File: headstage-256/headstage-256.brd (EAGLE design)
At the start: 32 x 32 mm, 291 parts, among them J2 MMCX-J-P-H-ST-SM1/U.FL-R-SMT(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, J4 PINHD-2X5+4DF40-HEAD, J5 5041940270, U1 OPA170, U10 NRF24L01QFN, U11 CAT4016_QFN, U12 CAT4016_QFN, U13 TPL0501_UQFN, U14 TPL0501_UQFN, U15 MICROSD_473093751, U16 10M08SAM15317G, U17 Si8487DB, U18 MAX17048_WLP, U19 BNO055, U2 OPA170, U20 TPS61202, U21 RHD2064_BGA, U22 RHD2064_BGA, U23 TS4231, U24 TS4231, U25 LT3463, U26 ASCO-50.000MHZ-EK-T3, U27 TS4231, U28 TLV70733, U29 TS4231, U3 INA826, U30 RHD2064_BGA, U31 RHD2064_BGA, U32 MIC23150, U33 TS4231, U34 TS4231, U35 TPS8268180, U4 INA826, U5 DAC5311, U6 DAC5311, U7 DS90UB913A_WQFN, U8 ADG1401, U9 ADG1401, Y1 FW1600008, Y2 ECS-.327-12.5-1210-TR

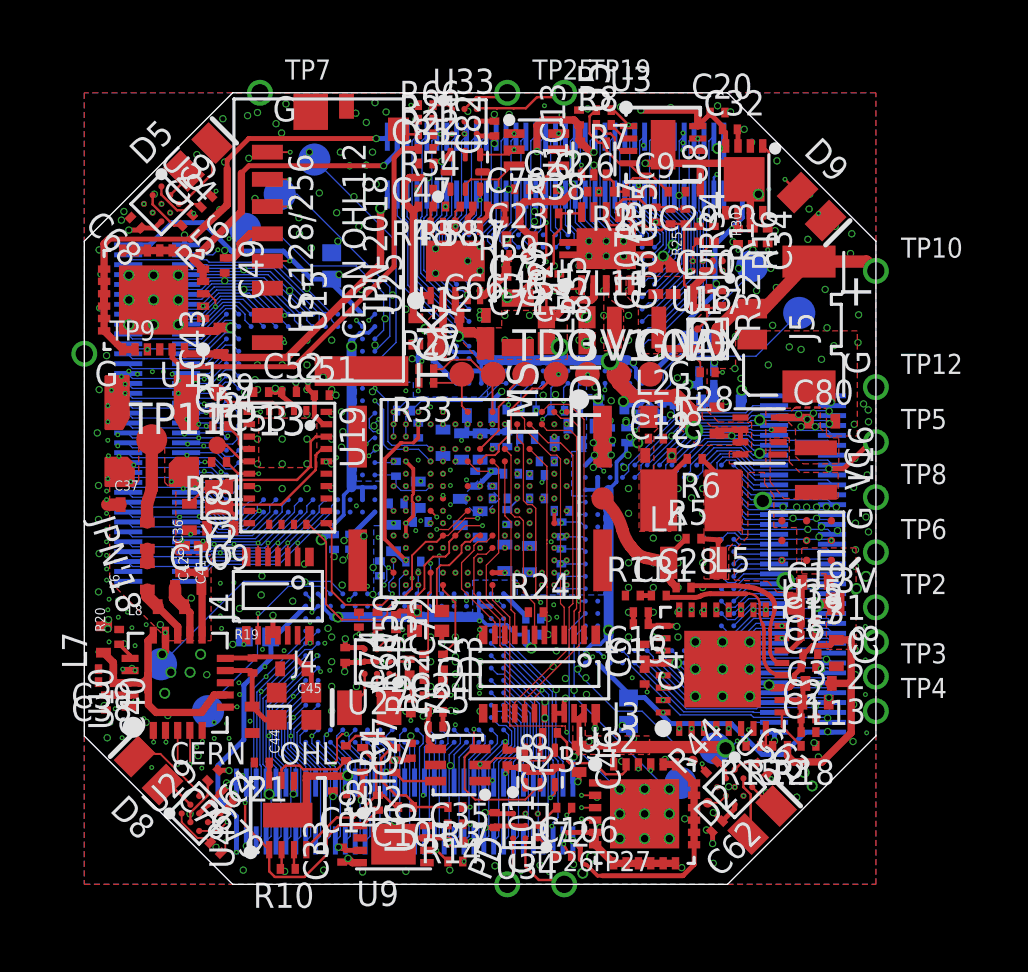
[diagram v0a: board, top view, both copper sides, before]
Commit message: Updates due to production questions from speedy
- Space added between some components
- 3.3V stub removed from headstage-64
- Intan AUXOUTs routed to test points on both boards
- Crystal's re-routed to drive FPGA clock pins that interface with an
avaialble PLL. Previous routing went to clock pins that had no PLL on
both designs.
- Some pins swapping to simplfy routing on both boards.
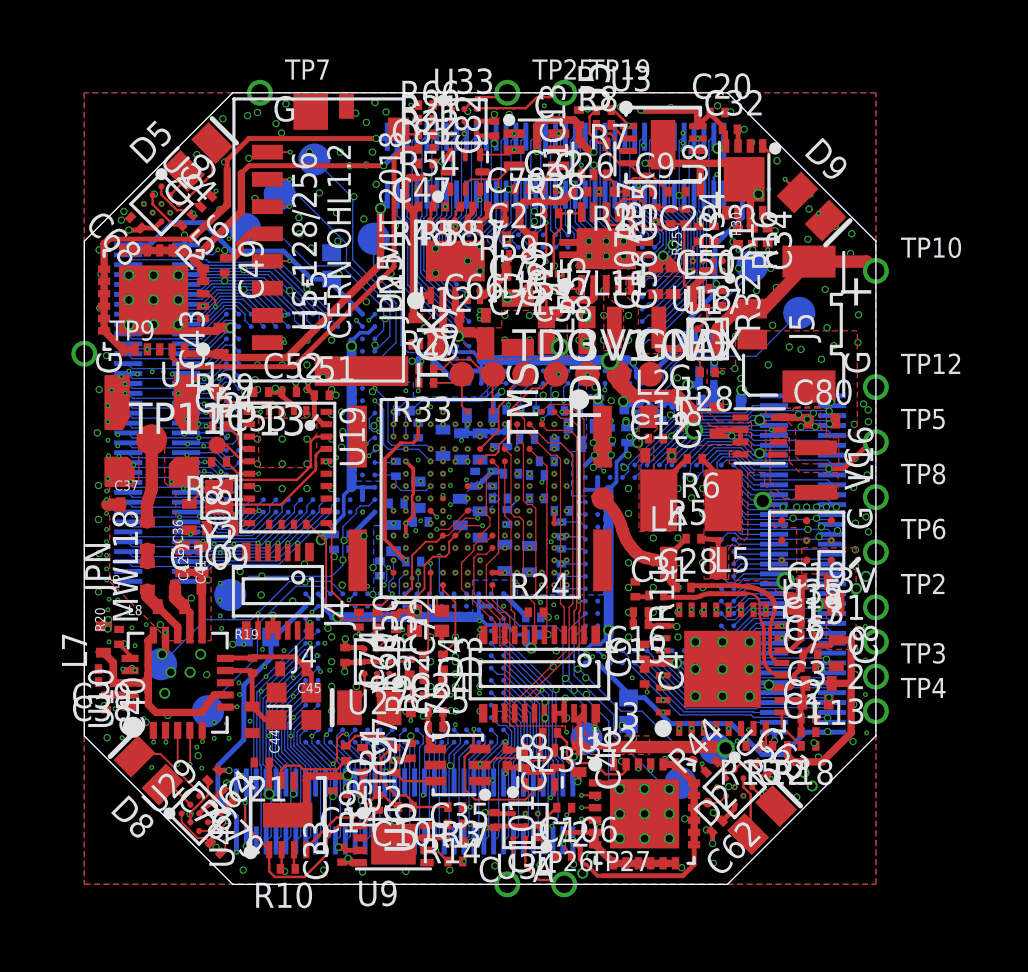
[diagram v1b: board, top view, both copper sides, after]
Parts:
- added TP30, TP31, TP32: (no value), jonnew:TP13R
- moved R11 0.27 mm to (6.28, -4.08), turned to 270 degrees
- moved J4 0.20 mm to (-8.18, -4.15)
- moved C31 0.10 mm to (7.12, -4.33)
- moved C60 0.10 mm to (-2.15, 5.16)
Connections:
- new net N$23: TP30.TP, U21.N16
- new net N$32: TP32.TP, U30.N16
- new net N$40: TP31.TP, U22.N16
- net N$22: now also U16.J5; no longer U16.H11
- net STIM_NULL_A: now also U16.H11; no longer U16.J5
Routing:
- net N$40: track 0.00 -> 8.44 mm
- net N$32: track 0.00 -> 8.41 mm
- net N$23: track 0.00 -> 8.38 mm
- net N$22: track 4.27 -> 6.70 mm, vias 0 -> 2
- net STIM_NULL_A: track 20.9 -> 22.7 mm
- net AGND: track 8.45 -> 8.09 mm, vias 266 -> 273
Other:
- board text added: "(C) JPN"
- board text added: "HS-128/256"
- board text added: "Headstage-256"
- board text added: "JPN MIT 2018"
- board text added: "JPN MWL18"
- board text added: "OUT"
- board text removed: "CERN"
- board text removed: "HS-128/256 JPN 2018"
- board text removed: "JPN'18"
- board text removed: "JPN, MIT"
- board text removed: "OHL"
- board text removed: "PD"
- board text removed: "headstage-256"

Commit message: Added AGND testpoints to bottom of headstage-64 and headstage-256
- So that people can actually use the other IO test points...
- These are ready for production
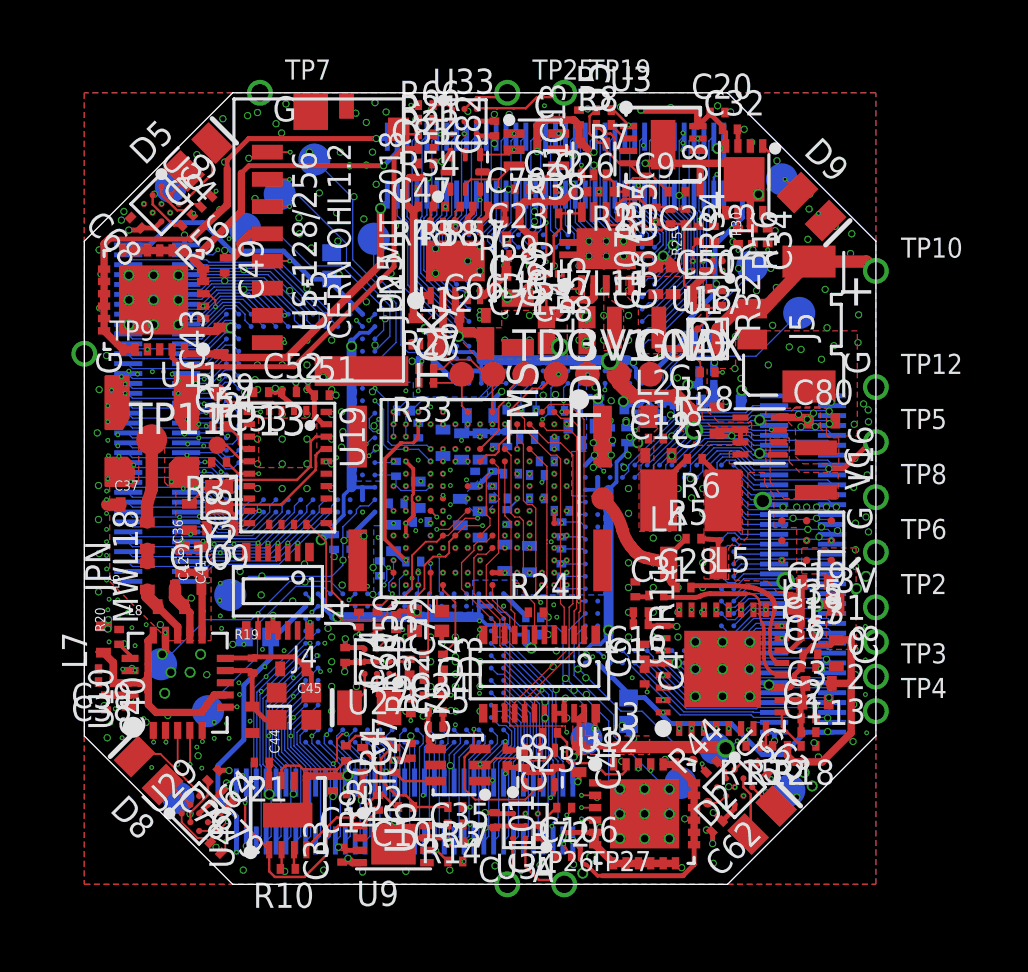
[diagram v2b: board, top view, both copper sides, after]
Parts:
- added TP33, TP34, TP35, TP36: (no value), jonnew:TP13R
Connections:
- net AGND: now also TP33.TP, TP34.TP, TP35.TP, TP36.TP
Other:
- board text added: "AG"
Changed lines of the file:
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@@
 <setting verticaltext="up"/>
 </settings>
-<grid distance="0.1" unitdist="mm" unit="mm" style="lines" multiple="1" display="yes" altdistance="0.025" altunitdist="inch" altunit="inch"/>
+<grid distance="0.25" unitdist="mm" unit="mm" style="lines" multiple="1" display="yes" altdistance="0.025" altunitdist="inch" altunit="inch"/>
 <layers>
 <layer number="1" name="Top" color="4" fill="1" visible="yes" active="yes"/>
@@
 <text x="-14.9" y="-3.15" size="1.016" layer="21" font="vector" ratio="18" distance="10" rot="R90" align="center">JPN
 MWL18</text>
-<text x="-6.05" y="11.4" size="1.016" layer="22" font="vector" ratio="18" rot="MR225" align="center">OUT</text>
-<text x="-11.4" y="-6.05" size="1.016" layer="22" font="vector" ratio="18" rot="MR135" align="center">OUT</text>
-<text x="6.05" y="-11.4" size="1.016" layer="22" font="vector" ratio="18" rot="SMR225" align="center">OUT</text>
+<text x="-11.3" y="-5.6" size="1.016" layer="22" font="vector" ratio="18" rot="SMR135" align="center">OUT</text>
+<text x="-11.4" y="-11" size="1.016" layer="22" font="vector" ratio="18" rot="SMR135" align="center">AG</text>
+<text x="5.6" y="-11.3" size="1.016" layer="22" font="vector" ratio="18" rot="SMR45" align="center">OUT</text>
+<text x="11.25" y="-11.65" size="1.016" layer="22" font="vector" ratio="18" rot="SMR45" align="center">G</text>
+<text x="11.3" y="5.6" size="1.016" layer="22" font="vector" ratio="18" rot="SMR315" align="center">OUT</text>
+<text x="11.4" y="11" size="1.016" layer="22" font="vector" ratio="18" rot="SMR315" align="center">AG</text>
+<text x="-5.6" y="11.3" size="1.016" layer="22" font="vector" ratio="18" rot="SMR225" align="center">OUT</text>
+<text x="-11.25" y="11.65" size="1.016" layer="22" font="vector" ratio="18" rot="SMR225" align="center">G</text>
 </plain>
 <attributes>
@@
 <element name="TP32" library="jonnew" package="TP13R" value="" x="4.3" y="-10.1" rot="MR0">
 <attribute name="TP_SIGNAL_NAME" value="" x="4.3" y="-10.1" size="1.778" layer="28" rot="MR0" display="off"/>
+</element>
+<element name="TP33" library="jonnew" package="TP13R" value="" x="-12.2" y="-12.5" rot="MR0">
+<attribute name="TP_SIGNAL_NAME" value="" x="-12.2" y="-12.5" size="1.778" layer="28" rot="MR0" display="off"/>
+</element>
+<element name="TP34" library="jonnew" package="TP13R" value="" x="12.5" y="-12.2" rot="MR0">
+<attribute name="TP_SIGNAL_NAME" value="" x="12.5" y="-12.2" size="1.778" layer="28" rot="MR0" display="off"/>
+</element>
+<element name="TP35" library="jonnew" package="TP13R" value="" x="12.2" y="12.5" rot="MR0">
+<attribute name="TP_SIGNAL_NAME" value="" x="12.2" y="12.5" size="1.778" layer="28" rot="MR0" display="off"/>
+</element>
+<element name="TP36" library="jonnew" package="TP13R" value="" x="-12.5" y="12.2" rot="MR0">
+<attribute name="TP_SIGNAL_NAME" value="" x="-12.5" y="12.2" size="1.778" layer="28" rot="MR0" display="off"/>
 </element>
 </elements>
@@
 <via x="3.5" y="-9.275" extent="5-16" drill="0.2"/>
 <via x="4.65" y="-11.175" extent="5-16" drill="0.2"/>
+<contactref element="TP33" pad="TP"/>
+<contactref element="TP34" pad="TP"/>
+<contactref element="TP35" pad="TP"/>
+<contactref element="TP36" pad="TP"/>
 </signal>
 <signal name="RHD_CS-_AC">

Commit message: Incrreased the value of the estim discharge resistor
- Circuit could become unstable if current still being passed when
analog switch was closed. This fixes this issue.
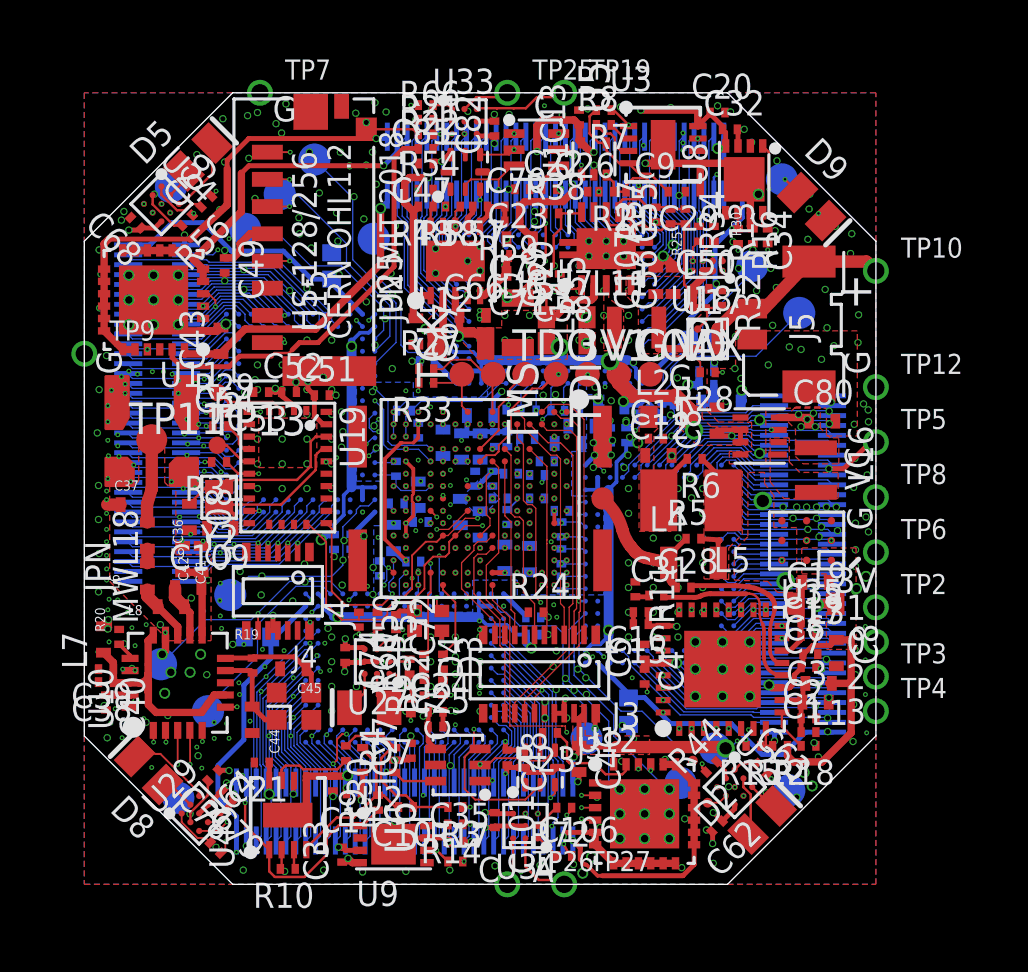
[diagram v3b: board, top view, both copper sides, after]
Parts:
- R13, R14: value 49.9 -> 590
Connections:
- removed net N$54: C9.1, R1.2, R2.1, U1.3
- removed net N$61: C10.1, R3.2, R4.1, U2.3
- new net ISTIM_MONO_A: C9.1, R1.2, R2.1, U1.3, U21.N5
- new net ISTIM_MONO_B: C10.1, R3.2, R4.1, U2.3, U30.N5
- net VDAC_A: no longer U21.N5
- net VDAC_B: no longer U30.N5
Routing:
- net ISTIM_MONO_A: track 0.00 -> 15.3 mm, vias 0 -> 4
- net VDAC_A: track 15.0 -> 2.33 mm, vias 5 -> 2
- net N$61: track 7.20 -> 0.00 mm
- net ISTIM_MONO_B: track 0.00 -> 7.20 mm
- net N$54: track 3.16 -> 0.00 mm
- net SD_DET: track 1.46 -> 2.18 mm

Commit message: Replaced stim null circuit on both headstages
- ADG140x was replaced with dg509b, which is a 2 circuit 1-to-4 mux.
This allows the electrode path to be completely disconnected from
stimulation circuitry during idle periods. During idle periods,
stimuluation output is shunted to ground through a dummy load so that
offsets to not develop large voltages during idle periods.
- Additionally, the inverting node of the estim current source amplifier
is sent to the intan chip instead of the DAC voltage. This gives a true
reflection of delivered current rather than just the control signal.
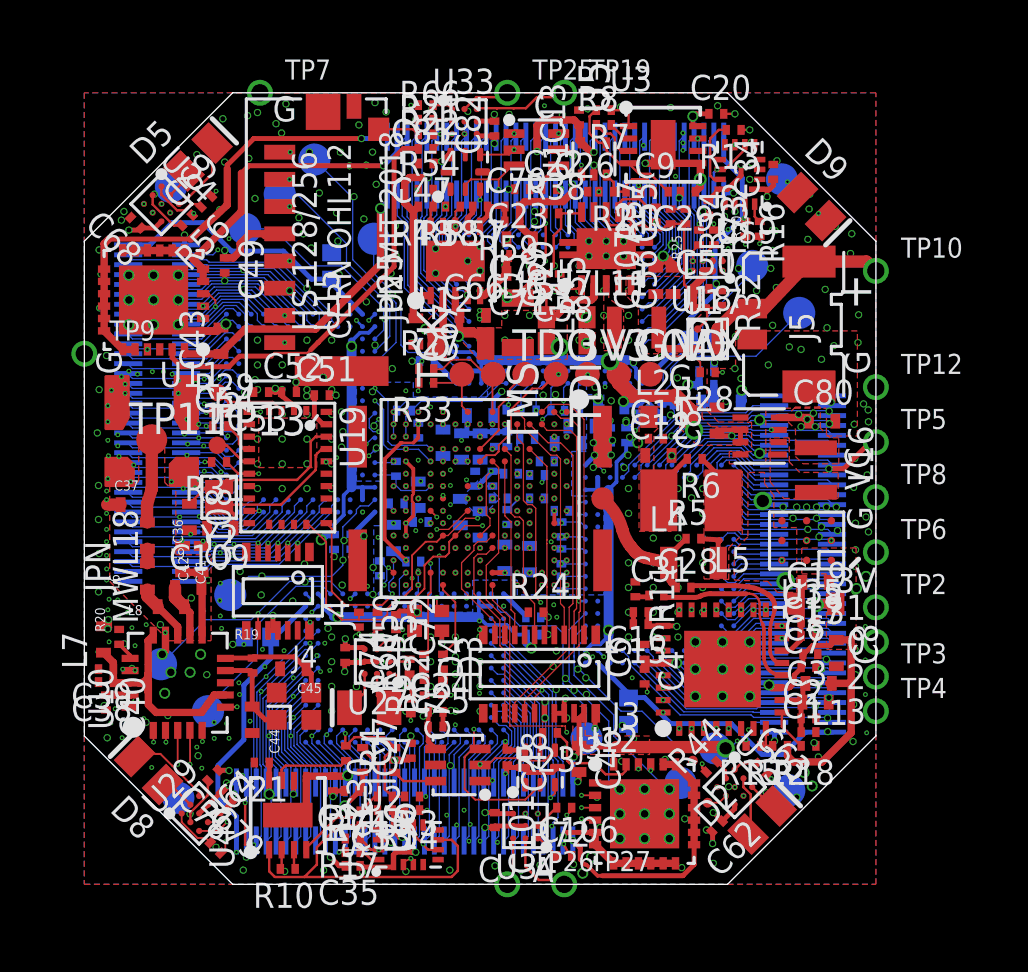
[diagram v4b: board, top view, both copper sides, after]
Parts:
- removed U8, U9: ADG1401, jonnew:LFCSP8-2X3
- added R73, R74: 10k, jonnew:0201T
- added U$22, U$9: (no value), jonnew:MQFN16-1.8X2.6
- moved R13 4.51 mm to (10.2, 14.5), turned to 180 degrees
- moved C35 4.26 mm to (-5.15, -15.2), turned to 180 degrees
- moved R17 4.25 mm to (-5.15, -14.2), turned to 180 degrees
- moved C32 3.29 mm to (9.22, 11.3), turned to 270 degrees
- moved C34 2.73 mm to (11.8, 12.8), turned to 90 degrees
- moved C33 2.49 mm to (-3.85, -13.0), turned to 180 degrees
- moved R14 1.84 mm to (-2.75, -13.0)
- moved R3 1.80 mm to (-2.75, -12.4)
- moved C10 0.95 mm to (-3.85, -12.4)
- moved R9 0.90 mm to (-4.80, -13.3)
- moved U15 0.50 mm to (-9.50, 9.75)
- moved R16 0.42 mm to (10.7, 10.5)
- moved C29 0.20 mm to (8.40, 12.0)
- moved R25 0.15 mm to (8.85, 10.2)
- moved R30 0.15 mm to (9.45, 10.2)
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- renumbered 3V1 to 3V3
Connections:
- new net ISTIM_A_PRE: R7.1, U$9.7, U3.1
- new net ISTIM_B_PRE: R9.1, U$22.7, U4.1
- new net N$31: R73.2, U$9.16
- new net N$41: R74.2, U$22.16
- net +15V0: now also U$22.12, U$9.12; no longer U8.4, U9.4
- net +3V3: now also R73.1, R74.1
- net -15V0: now also U$22.1, U$9.1; no longer U8.7, U8.PAD, U9.7, U9.PAD
- net GND: now also U$22.13, U$22.14, U$22.2, U$22.3, U$9.13, U$9.14, U$9.2; no longer U8.3, U9.3
- net ISTIM_A: now also U$9.10, U$9.6; no longer R7.1, U3.1, U8.1
- net ISTIM_B: now also U$22.10, U$22.6; no longer R9.1, U4.1, U9.1
- net N$55: now also U$9.11; no longer U8.8
- net N$62: now also U$22.11; no longer U9.8
- net STIM_NULL_A: now also U$9.15; no longer U8.6
- net STIM_NULL_B: now also U$22.15; no longer U9.6
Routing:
- net ISTIM_B_PRE: track 0.00 -> 14.3 mm
- net VDAC_B: track 13.5 -> 2.23 mm, vias 4 -> 0
- net ISTIM_A: track 11.1 -> 2.72 mm, vias 3 -> 1
- net ISTIM_A_PRE: track 0.00 -> 6.29 mm, vias 0 -> 2
- net ISTIM_MONO_B: track 7.20 -> 11.6 mm, vias 0 -> 2
- net GND: track 40.7 -> 43.0 mm, vias 406 -> 417
- net N$55: track 0.73 -> 2.76 mm
- net ISTIM_B: track 10.0 -> 11.8 mm, vias 1 -> 3
- net STIM_NULL_B: track 14.3 -> 15.8 mm
- net -15V0: track 73.0 -> 74.2 mm
- net +3V3: track 35.2 -> 36.3 mm, vias 48 -> 50
- net N$60: track 7.01 -> 6.04 mm
- net N$41: track 0.00 -> 0.87 mm
- net N$31: track 0.00 -> 0.78 mm
- net +15V0: track 86.0 -> 86.6 mm
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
